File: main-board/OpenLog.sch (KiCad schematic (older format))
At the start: 0 parts

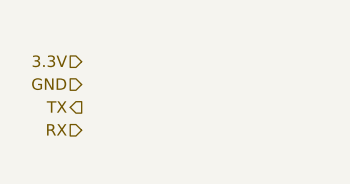
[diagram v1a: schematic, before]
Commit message: Subsheets
Added motor drivers, cooling fans, and openlog
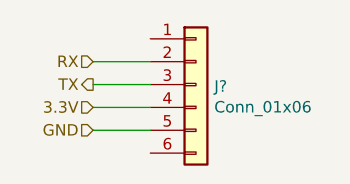
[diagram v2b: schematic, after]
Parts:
- added J?: Conn_01x06, symbol Connector_Generic:Conn_01x06
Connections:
- net 3.3V: now also J?.4 (Pin_4)
- net GND: now also J?.5 (Pin_5)
- net RX: now also J?.2 (Pin_2)
- net TX: now also J?.3 (Pin_3)
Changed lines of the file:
@@
 EESchema Schematic File Version 4
+LIBS:main-board-cache
 EELAYER 30 0
 EELAYER END
@@
 Comment4 ""
 $EndDescr
-Text HLabel 4600 3650 0    50   Input ~ 0
+Text HLabel 4650 3850 0    50   Input ~ 0
 3.3V
-Text HLabel 4600 3750 0    50   Input ~ 0
+Text HLabel 4650 3950 0    50   Input ~ 0
 GND
-Text HLabel 4600 3850 0    50   Output ~ 0
+Text HLabel 4650 3750 0    50   Output ~ 0
 TX
-Text HLabel 4600 3950 0    50   Input ~ 0
+Text HLabel 4650 3650 0    50   Input ~ 0
 RX
+$Comp
+L Connector_Generic:Conn_01x06 J?
+U 1 1 60B20018
+P 5100 3750
+F 0 "J?" H 5180 3742 50  0000 L CNN
+F 1 "Conn_01x06" H 5180 3651 50  0000 L CNN
+F 2 "" H 5100 3750 50  0001 C CNN
+F 3 "~" H 5100 3750 50  0001 C CNN
+	1    5100 3750
+	1    0    0    -1
+$EndComp
+Wire Wire Line
+	4900 3650 4650 3650
+Wire Wire Line
+	4900 3750 4650 3750
+Wire Wire Line
+	4650 3850 4900 3850
+Wire Wire Line
+	4900 3950 4650 3950
 $EndSCHEMATC
